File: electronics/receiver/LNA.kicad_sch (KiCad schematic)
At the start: 25 parts, among them J407 Conn_Coaxial, U407 AS179-92LF, U408 PSA4-5043, U409 AS179-92LF

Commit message: Add values
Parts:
- C413, C414, C415, C416, C419, C421, C422, C423, C424: value C -> 1n0
- C420: value C -> 100n
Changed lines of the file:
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@@
       (effects (font (size 1.27 1.27)) (justify left))
     )
-    (property "Value" "C" (id 1) (at 251.8922 77.089 0)
+    (property "Value" "1n0" (id 1) (at 251.8922 77.089 0)
       (effects (font (size 1.27 1.27)) (justify left))
     )
@@
   (symbol (lib_id "Device:C") (at 118.11 85.09 0) (unit 1)
     (in_bom yes) (on_board yes) (fields_autoplaced)
-    (property "Reference" "C418" (id 0) (at 121.031 84.1815 0)
-      (effects (font (size 1.27 1.27)) (justify left))
-    )
-    (property "Value" "C" (id 1) (at 121.031 86.9566 0)
+    (property "Reference" "C418" (id 0) (at 121.92 83.8199 0)
+      (effects (font (size 1.27 1.27)) (justify left))
+    )
+    (property "Value" "C" (id 1) (at 121.92 86.3599 0)
       (effects (font (size 1.27 1.27)) (justify left))
     )
@@
     (in_bom yes) (on_board yes) (fields_autoplaced)
     (property "Reference" "C414" (id 0) (at 54.61 77.9612 90))
-    (property "Value" "C" (id 1) (at 54.61 80.4981 90))
+    (property "Value" "1n0" (id 1) (at 54.61 80.4981 90))
     (property "Footprint" "Capacitor_SMD:C_0805_2012Metric_Pad1.18x1.45mm_HandSolder" (id 2) (at 58.42 82.8548 0)
       (effects (font (size 1.27 1.27)) hide)
@@
     (in_bom yes) (on_board yes) (fields_autoplaced)
     (property "Reference" "C419" (id 0) (at 124.46 71.3445 90))
-    (property "Value" "C" (id 1) (at 124.46 74.1196 90))
+    (property "Value" "1n0" (id 1) (at 124.46 74.1196 90))
     (property "Footprint" "Capacitor_SMD:C_0805_2012Metric" (id 2) (at 120.65 78.4352 0)
       (effects (font (size 1.27 1.27)) hide)
@@
     (in_bom yes) (on_board yes) (fields_autoplaced)
     (property "Reference" "C416" (id 0) (at 97.79 71.3445 90))
-    (property "Value" "C" (id 1) (at 97.79 74.1196 90))
+    (property "Value" "1n0" (id 1) (at 97.79 74.1196 90))
     (property "Footprint" "Capacitor_SMD:C_0805_2012Metric" (id 2) (at 93.98 78.4352 0)
       (effects (font (size 1.27 1.27)) hide)
@@
     (in_bom yes) (on_board yes) (fields_autoplaced)
     (property "Reference" "C415" (id 0) (at 86.36 80.2345 90))
-    (property "Value" "C" (id 1) (at 86.36 83.0096 90))
+    (property "Value" "1n0" (id 1) (at 86.36 83.0096 90))
     (property "Footprint" "Capacitor_SMD:C_0805_2012Metric" (id 2) (at 90.17 87.3252 0)
       (effects (font (size 1.27 1.27)) hide)
@@
     (in_bom yes) (on_board yes) (fields_autoplaced)
     (property "Reference" "C413" (id 0) (at 33.02 77.6945 90))
-    (property "Value" "C" (id 1) (at 33.02 80.4696 90))
+    (property "Value" "1n0" (id 1) (at 33.02 80.4696 90))
     (property "Footprint" "Capacitor_SMD:C_0805_2012Metric_Pad1.18x1.45mm_HandSolder" (id 2) (at 36.83 82.8548 0)
       (effects (font (size 1.27 1.27)) hide)
@@
       (effects (font (size 1.27 1.27)) (justify left))
     )
-    (property "Value" "C" (id 1) (at 206.5778 80.391 0)
+    (property "Value" "1n0" (id 1) (at 206.5778 80.391 0)
       (effects (font (size 1.27 1.27)) (justify left))
     )
@@
   (symbol (lib_id "Device:C") (at 146.05 63.5 0) (unit 1)
     (in_bom yes) (on_board yes) (fields_autoplaced)
-    (property "Reference" "C420" (id 0) (at 148.971 62.5915 0)
-      (effects (font (size 1.27 1.27)) (justify left))
-    )
-    (property "Value" "C" (id 1) (at 148.971 65.3666 0)
+    (property "Reference" "C420" (id 0) (at 149.86 62.2299 0)
+      (effects (font (size 1.27 1.27)) (justify left))
+    )
+    (property "Value" "100n" (id 1) (at 149.86 64.7699 0)
       (effects (font (size 1.27 1.27)) (justify left))
     )
@@
       (effects (font (size 1.27 1.27)) (justify left))
     )
-    (property "Value" "C" (id 1) (at 212.471 99.4922 0)
+    (property "Value" "1n0" (id 1) (at 212.471 99.4922 0)
       (effects (font (size 1.27 1.27)) (justify left))
     )
@@
   (symbol (lib_id "Device:C") (at 105.41 85.09 0) (unit 1)
     (in_bom yes) (on_board yes) (fields_autoplaced)
-    (property "Reference" "C417" (id 0) (at 108.331 84.1815 0)
-      (effects (font (size 1.27 1.27)) (justify left))
-    )
-    (property "Value" "C" (id 1) (at 108.331 86.9566 0)
+    (property "Reference" "C417" (id 0) (at 109.22 83.8199 0)
+      (effects (font (size 1.27 1.27)) (justify left))
+    )
+    (property "Value" "C" (id 1) (at 109.22 86.3599 0)
       (effects (font (size 1.27 1.27)) (justify left))
     )
@@
     (in_bom yes) (on_board yes) (fields_autoplaced)
     (property "Reference" "C421" (id 0) (at 158.75 71.3445 90))
-    (property "Value" "C" (id 1) (at 158.75 74.1196 90))
+    (property "Value" "1n0" (id 1) (at 158.75 74.1196 90))
     (property "Footprint" "Capacitor_SMD:C_0805_2012Metric" (id 2) (at 162.56 76.5048 0)
       (effects (font (size 1.27 1.27)) hide)

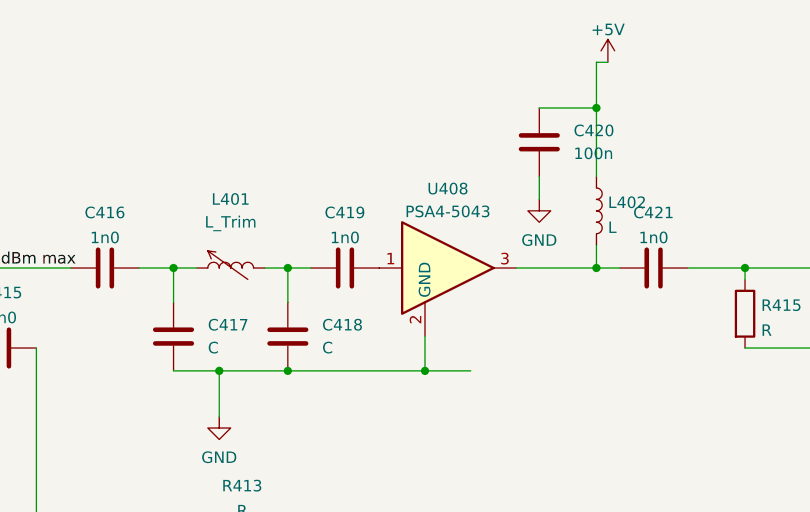
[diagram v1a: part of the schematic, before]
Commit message: Branch for changes to RX LNA board from M0SKP
Upgrade files to Kicad 7
Added Fields for comment and LCSC part numbers to symbol table
Populated some LCSC part numbers to allow testing at JLCPCB
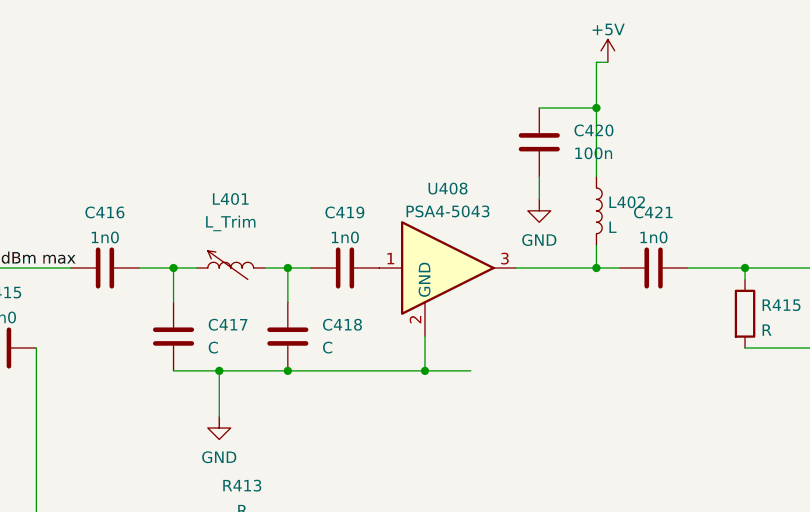
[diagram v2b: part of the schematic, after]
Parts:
- C413, C414, C415, C416, C419, C421, C422, C423, C424: Comment (none) -> Ceramic Capacitor 1nf 50V 5% 0805; LCSC Part (none) -> C62774
- C420: Comment (none) -> Ceramic Capacitor 100nf 50V 5% 0805; LCSC Part (none) -> C111492
- D401: Comment (none) -> PIN Limiter diode Dual series SOT-23; LCSC Part (none) -> C150870
- U407, U409: Comment (none) -> SPDT RF Switch SOT363; LCSC Part (none) -> C83422
- U408: Comment (none) -> Low Noise Amplifer SOT343; LCSC Part (none) -> C5240848
